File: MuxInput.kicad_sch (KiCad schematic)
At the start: 2 parts

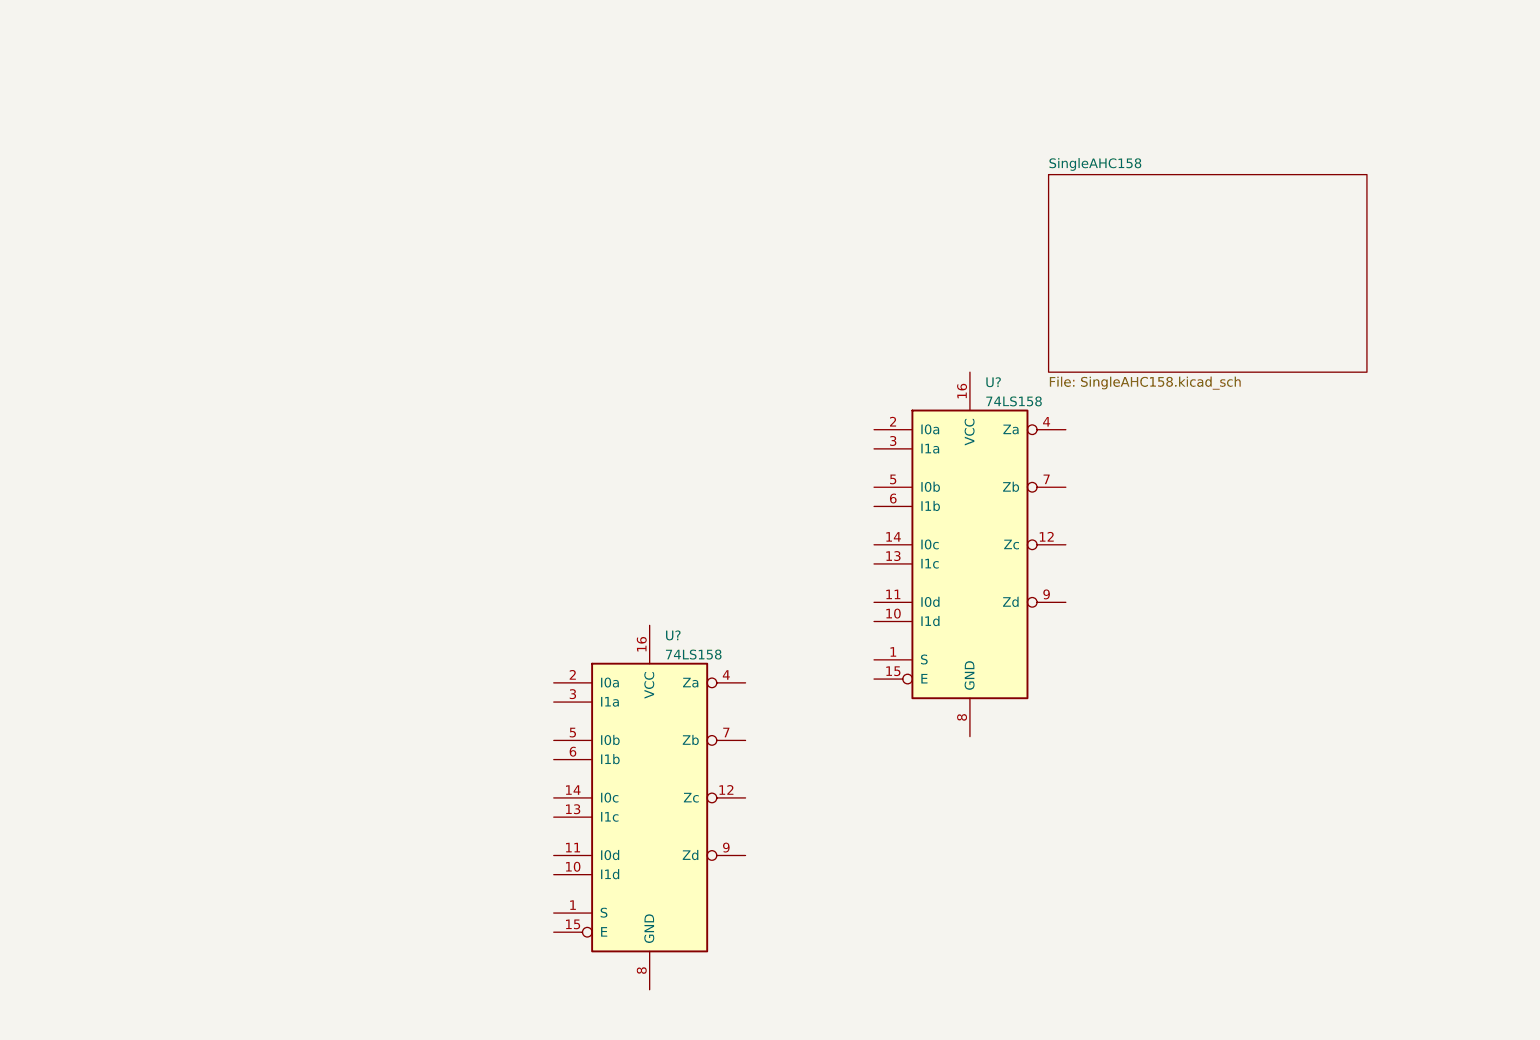
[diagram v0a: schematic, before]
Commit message: Got the address muxer finished
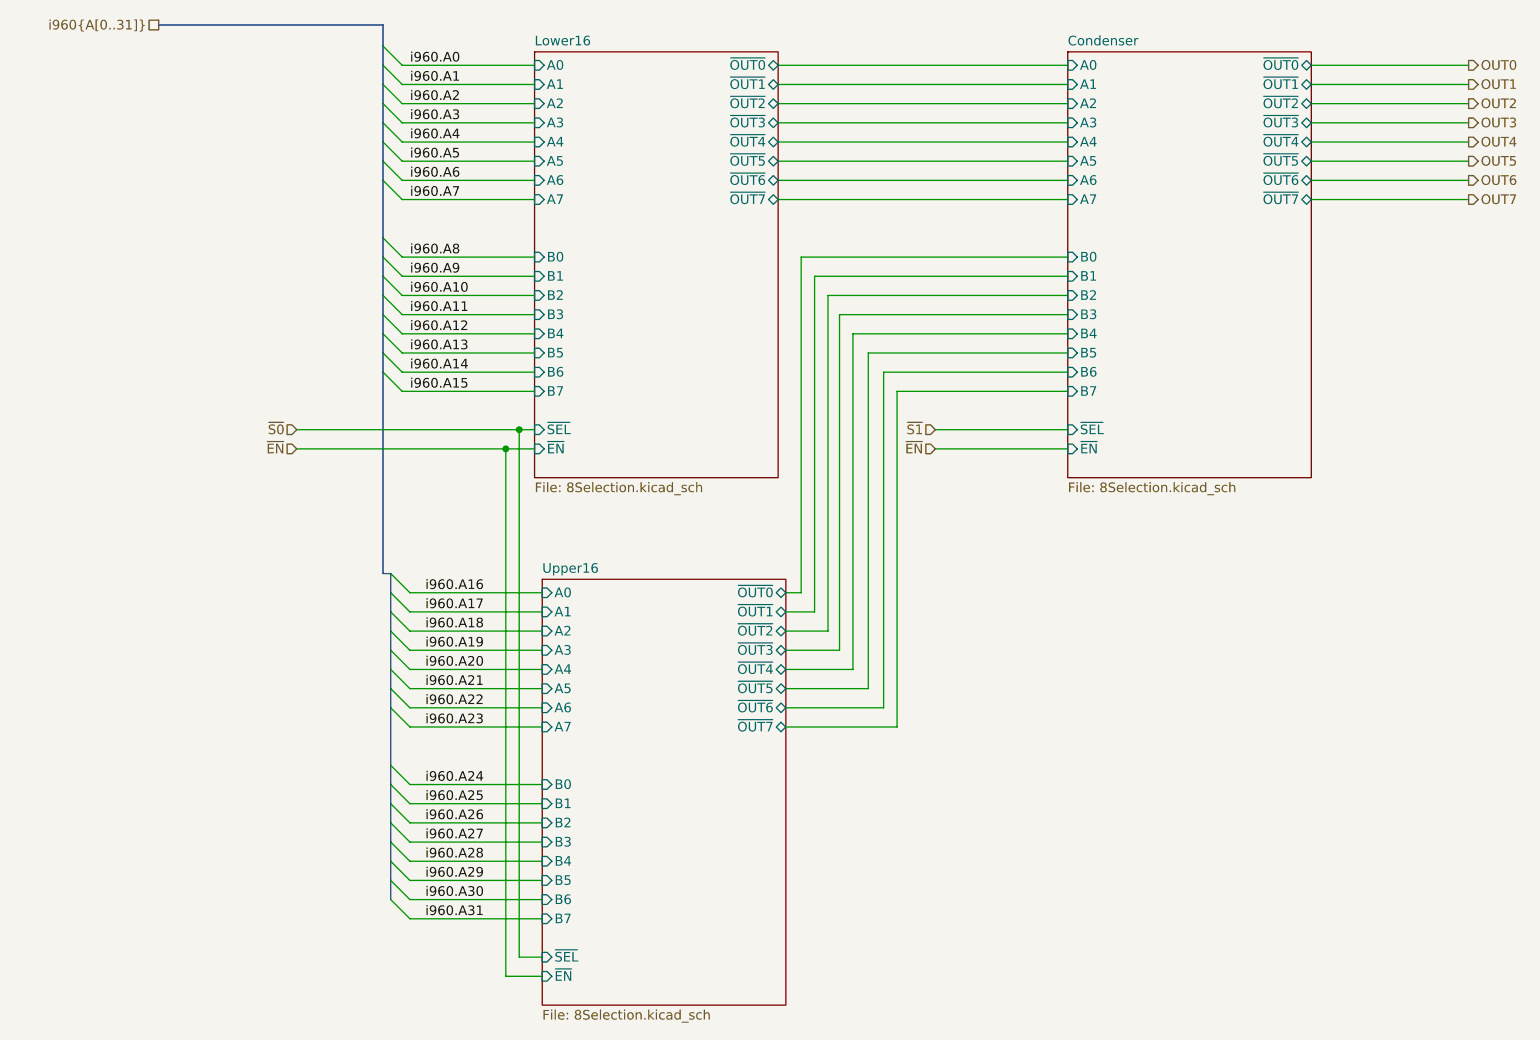
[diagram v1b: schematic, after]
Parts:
- removed U? (x2): 74LS158, symbol 74xx:74LS158
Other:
- removed sheet SingleAHC158
- added sheet Condenser (8Selection.kicad_sch)
- added sheet Lower16 (8Selection.kicad_sch)
- added sheet Upper16 (8Selection.kicad_sch)

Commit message: Use bus lines for logic level conversion
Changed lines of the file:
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@@
+    (stroke (width 0) (type default) (color 0 0 0 0))
+  )
+  (bus_entry (at 207.772 44.196) (size 2.54 -2.54)
     (stroke (width 0) (type default) (color 0 0 0 0))
   )
@@
     (stroke (width 0) (type default) (color 0 0 0 0))
   )
+  (bus_entry (at 207.772 36.576) (size 2.54 -2.54)
+    (stroke (width 0) (type default) (color 0 0 0 0))
+  )
   (bus_entry (at 65.024 136.906) (size 2.54 2.54)
     (stroke (width 0) (type default) (color 0 0 0 0))
   )
+  (bus_entry (at 207.772 34.036) (size 2.54 -2.54)
+    (stroke (width 0) (type default) (color 0 0 0 0))
+  )
   (bus_entry (at 65.024 106.426) (size 2.54 2.54)
     (stroke (width 0) (type default) (color 0 0 0 0))
@@
     (stroke (width 0) (type default) (color 0 0 0 0))
   )
+  (bus_entry (at 207.772 46.736) (size 2.54 -2.54)
+    (stroke (width 0) (type default) (color 0 0 0 0))
+  )
   (bus_entry (at 65.024 131.826) (size 2.54 2.54)
     (stroke (width 0) (type default) (color 0 0 0 0))
@@
     (stroke (width 0) (type default) (color 0 0 0 0))
   )
+  (bus_entry (at 207.772 41.656) (size 2.54 -2.54)
+    (stroke (width 0) (type default) (color 0 0 0 0))
+  )
   (bus_entry (at 64.008 54.356) (size 2.54 2.54)
     (stroke (width 0) (type default) (color 0 0 0 0))
@@
     (stroke (width 0) (type default) (color 0 0 0 0))
   )
+  (bus_entry (at 207.772 31.496) (size 2.54 -2.54)
+    (stroke (width 0) (type default) (color 0 0 0 0))
+  )
   (bus_entry (at 64.008 31.496) (size 2.54 2.54)
     (stroke (width 0) (type default) (color 0 0 0 0))
@@
     (stroke (width 0) (type default) (color 0 0 0 0))
   )
+  (bus_entry (at 207.772 28.956) (size 2.54 -2.54)
+    (stroke (width 0) (type default) (color 0 0 0 0))
+  )
   (bus_entry (at 64.008 44.196) (size 2.54 2.54)
     (stroke (width 0) (type default) (color 0 0 0 0))
   )
+  (bus_entry (at 207.772 39.116) (size 2.54 -2.54)
+    (stroke (width 0) (type default) (color 0 0 0 0))
+  )
   (bus_entry (at 65.024 139.446) (size 2.54 2.54)
     (stroke (width 0) (type default) (color 0 0 0 0))
@@
     (stroke (width 0) (type default) (color 0 0 0 0))
   )
+  (bus (pts (xy 210.312 31.496) (xy 210.312 28.956))
+    (stroke (width 0) (type default) (color 0 0 0 0))
+  )
   (wire (pts (xy 186.944 39.116) (xy 207.772 39.116))
     (stroke (width 0) (type default) (color 0 0 0 0))
@@
     (stroke (width 0) (type default) (color 0 0 0 0))
   )
+  (bus (pts (xy 210.312 26.416) (xy 210.312 22.352))
+    (stroke (width 0) (type default) (color 0 0 0 0))
+  )
   (wire (pts (xy 66.548 34.036) (xy 84.074 34.036))
     (stroke (width 0) (type default) (color 0 0 0 0))
@@
     (stroke (width 0) (type default) (color 0 0 0 0))
   )
+  (bus (pts (xy 210.312 22.352) (xy 227.33 22.352))
+    (stroke (width 0) (type default) (color 0 0 0 0))
+  )
   (wire (pts (xy 126.238 64.516) (xy 154.686 64.516))
     (stroke (width 0) (type default) (color 0 0 0 0))
@@
     (stroke (width 0) (type default) (color 0 0 0 0))
   )
+  (bus (pts (xy 210.312 28.956) (xy 210.312 26.416))
+    (stroke (width 0) (type default) (color 0 0 0 0))
+  )
+  (bus (pts (xy 210.312 36.576) (xy 210.312 34.036))
+    (stroke (width 0) (type default) (color 0 0 0 0))
+  )
   (bus (pts (xy 65.024 98.806) (xy 65.024 101.346))
     (stroke (width 0) (type default) (color 0 0 0 0))
@@
     (stroke (width 0) (type default) (color 0 0 0 0))
   )
+  (bus (pts (xy 210.312 44.196) (xy 210.312 41.656))
+    (stroke (width 0) (type default) (color 0 0 0 0))
+  )
   (wire (pts (xy 117.348 103.886) (xy 122.936 103.886))
     (stroke (width 0) (type default) (color 0 0 0 0))
@@
     (stroke (width 0) (type default) (color 0 0 0 0))
   )
+  (bus (pts (xy 210.312 39.116) (xy 210.312 36.576))
+    (stroke (width 0) (type default) (color 0 0 0 0))
+  )
   (wire (pts (xy 80.264 79.756) (xy 80.264 149.606))
     (stroke (width 0) (type default) (color 0 0 0 0))
@@
     (stroke (width 0) (type default) (color 0 0 0 0))
   )
+  (bus (pts (xy 210.312 41.656) (xy 210.312 39.116))
+    (stroke (width 0) (type default) (color 0 0 0 0))
+  )
   (wire (pts (xy 119.38 54.356) (xy 154.686 54.356))
     (stroke (width 0) (type default) (color 0 0 0 0))
@@
     (stroke (width 0) (type default) (color 0 0 0 0))
   )
+  (bus (pts (xy 210.312 34.036) (xy 210.312 31.496))
+    (stroke (width 0) (type default) (color 0 0 0 0))
+  )
   (wire (pts (xy 116.332 44.196) (xy 154.686 44.196))
     (stroke (width 0) (type default) (color 0 0 0 0))
@@
     (effects (font (size 1.27 1.27)) (justify left bottom))
   )
+  (label "MUX.S0" (at 52.578 77.216 0)
+    (effects (font (size 1.27 1.27)) (justify left bottom))
+  )
   (label "i960.A4" (at 67.564 39.116 0)
     (effects (font (size 1.27 1.27)) (justify left bottom))
   )
+  (label "MUX.A0" (at 204.978 28.956 180)
+    (effects (font (size 1.27 1.27)) (justify right bottom))
+  )
+  (label "MUX.A5" (at 204.978 41.656 180)
+    (effects (font (size 1.27 1.27)) (justify right bottom))
+  )
   (label "i960.A28" (at 69.596 134.366 0)
     (effects (font (size 1.27 1.27)) (justify left bottom))
@@
     (effects (font (size 1.27 1.27)) (justify left bottom))
   )
+  (label "MUX.S1" (at 137.16 77.216 0)
+    (effects (font (size 1.27 1.27)) (justify left bottom))
+  )
   (label "i960.A5" (at 67.564 41.656 0)
     (effects (font (size 1.27 1.27)) (justify left bottom))
   )
+  (label "MUX.A3" (at 204.978 36.576 180)
+    (effects (font (size 1.27 1.27)) (justify right bottom))
+  )
   (label "i960.A18" (at 69.596 103.886 0)
     (effects (font (size 1.27 1.27)) (justify left bottom))
@@
     (effects (font (size 1.27 1.27)) (justify left bottom))
   )
+  (label "MUX.A1" (at 204.978 31.496 180)
+    (effects (font (size 1.27 1.27)) (justify right bottom))
+  )
   (label "i960.A29" (at 69.596 136.906 0)
     (effects (font (size 1.27 1.27)) (justify left bottom))
@@
     (effects (font (size 1.27 1.27)) (justify left bottom))
   )
+  (label "MUX.A6" (at 204.978 44.196 180)
+    (effects (font (size 1.27 1.27)) (justify right bottom))
+  )
   (label "i960.A3" (at 67.564 36.576 0)
     (effects (font (size 1.27 1.27)) (justify left bottom))
@@
     (effects (font (size 1.27 1.27)) (justify left bottom))
   )
+  (label "MUX.A2" (at 204.978 34.036 180)
+    (effects (font (size 1.27 1.27)) (justify right bottom))
+  )
   (label "i960.A26" (at 69.596 129.286 0)
     (effects (font (size 1.27 1.27)) (justify left bottom))
@@
     (effects (font (size 1.27 1.27)) (justify left bottom))
   )
+  (label "MUX.A4" (at 204.978 39.116 180)
+    (effects (font (size 1.27 1.27)) (justify right bottom))
+  )
   (label "i960.A31" (at 69.596 141.986 0)
     (effects (font (size 1.27 1.27)) (justify left bottom))
@@
     (effects (font (size 1.27 1.27)) (justify left bottom))
   )
+  (label "MUX.A7" (at 204.978 46.736 180)
+    (effects (font (size 1.27 1.27)) (justify right bottom))
+  )
   (label "i960.A25" (at 69.596 126.746 0)
     (effects (font (size 1.27 1.27)) (justify left bottom))
@@
   (label "i960.A6" (at 67.564 44.196 0)
     (effects (font (size 1.27 1.27)) (justify left bottom))
-  )
-  (hierarchical_label "OUT3" (shape output) (at 207.772 36.576 0)
-    (effects (font (size 1.27 1.27)) (justify left))
-  )
-  (hierarchical_label "OUT2" (shape output) (at 207.772 34.036 0)
-    (effects (font (size 1.27 1.27)) (justify left))
   )
   (hierarchical_label "~{EN}" (shape input) (at 52.578 79.756 180)
@@
     (effects (font (size 1.27 1.27)) (justify right))
   )
-  (hierarchical_label "OUT7" (shape output) (at 207.772 46.736 0)
+  (hierarchical_label "MUX{A[0..7],S[0..1]}" (shape passive) (at 227.33 22.352 0)
     (effects (font (size 1.27 1.27)) (justify left))
   )
-  (hierarchical_label "~{S1}" (shape input) (at 137.16 77.216 180)
-    (effects (font (size 1.27 1.27)) (justify right))
-  )
-  (hierarchical_label "OUT6" (shape output) (at 207.772 44.196 0)
-    (effects (font (size 1.27 1.27)) (justify left))
-  )
-  (hierarchical_label "OUT5" (shape output) (at 207.772 41.656 0)
-    (effects (font (size 1.27 1.27)) (justify left))
-  )
-  (hierarchical_label "~{S0}" (shape input) (at 52.578 77.216 180)
-    (effects (font (size 1.27 1.27)) (justify right))
-  )
-  (hierarchical_label "OUT4" (shape output) (at 207.772 39.116 0)
-    (effects (font (size 1.27 1.27)) (justify left))
-  )
-  (hierarchical_label "OUT1" (shape output) (at 207.772 31.496 0)
-    (effects (font (size 1.27 1.27)) (justify left))
-  )
-  (hierarchical_label "OUT0" (shape output) (at 207.772 28.956 0)
-    (effects (font (size 1.27 1.27)) (justify left))
-  )

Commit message: Update everything and keep laying out the i960 features
Use bus wires as much as possible
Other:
- company: (none) -> Joshua Scoggins
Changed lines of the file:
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@@
 (kicad_sch (version 20211123) (generator eeschema)
   (paper "A3")
+  (title_block
+    (date "2022-05-13")
+    (rev "1")
+    (company "Joshua Scoggins")
+  )
   (junction (at 82.042 77.216) (diameter 0) (color 0 0 0 0)
   )
